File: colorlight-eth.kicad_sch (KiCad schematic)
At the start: 8 parts, among them J1 Conn_02x15_Odd_Even, J2 2250013-4, J4 Conn_01x05_Male, J5 2250013-4

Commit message: v1.2 : fix 5V feed to magnetics
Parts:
- added JP1: SolderJumper_3_Open, Jumper:SolderJumper-3_P1.3mm_Open_RoundedPad1.0x1.5mm, symbol keyboard-rescue:SolderJumper_3_Open-Jumper
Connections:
- net 0V: no longer J1.15 (Pin_15)
- net 3V3: now also JP1.1 (A); no longer J2.2 (VCC), J5.2 (VCC)
- new net 5V: J1.15 (Pin_15), JP1.3 (B)
- new net Vcc: J2.2 (VCC), J5.2 (VCC), JP1.2 (C)
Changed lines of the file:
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@@
   (no_connect (at 211.582 88.392))
   (no_connect (at 110.744 67.818))
+  (wire (pts (xy 124.587 117.729) (xy 128.397 117.729))
+    (stroke (width 0) (type default) (color 0 0 0 0))
+  )
   (wire (pts (xy 208.788 50.292) (xy 211.582 50.292))
     (stroke (width 0) (type default) (color 0 0 0 0))
@@
     (stroke (width 0) (type default) (color 0 0 0 0))
   )
+  (wire (pts (xy 128.397 112.649) (xy 132.08 112.649))
+    (stroke (width 0) (type default) (color 0 0 0 0))
+  )
+  (wire (pts (xy 128.397 115.189) (xy 132.08 115.189))
+    (stroke (width 0) (type default) (color 0 0 0 0))
+  )
   (wire (pts (xy 95.758 60.198) (xy 98.044 60.198))
     (stroke (width 0) (type default) (color 0 0 0 0))
@@
     (stroke (width 0) (type default) (color 0 0 0 0))
   )
+  (wire (pts (xy 128.397 107.569) (xy 128.397 110.109))
+    (stroke (width 0) (type default) (color 0 0 0 0))
+  )
   (wire (pts (xy 208.788 93.472) (xy 211.582 93.472))
     (stroke (width 0) (type default) (color 0 0 0 0))
   )
-  (wire (pts (xy 149.606 38.608) (xy 152.4 38.608))
-    (stroke (width 0) (type default) (color 0 0 0 0))
-  )
   (wire (pts (xy 198.628 74.422) (xy 199.898 74.422))
     (stroke (width 0) (type default) (color 0 0 0 0))
@@
     (stroke (width 0) (type default) (color 0 0 0 0))
   )
+  (wire (pts (xy 128.397 110.109) (xy 132.08 110.109))
+    (stroke (width 0) (type default) (color 0 0 0 0))
+  )
   (wire (pts (xy 208.788 75.692) (xy 211.582 75.692))
     (stroke (width 0) (type default) (color 0 0 0 0))
@@
     (stroke (width 0) (type default) (color 0 0 0 0))
   )
+  (wire (pts (xy 128.397 117.729) (xy 128.397 115.189))
+    (stroke (width 0) (type default) (color 0 0 0 0))
+  )
   (wire (pts (xy 199.898 74.422) (xy 199.898 75.692))
     (stroke (width 0) (type default) (color 0 0 0 0))
@@
     (stroke (width 0) (type default) (color 0 0 0 0))
   )
+  (wire (pts (xy 149.352 38.608) (xy 152.4 38.608))
+    (stroke (width 0) (type default) (color 0 0 0 0))
+  )
   (wire (pts (xy 208.788 73.152) (xy 211.582 73.152))
     (stroke (width 0) (type default) (color 0 0 0 0))
@@
     (stroke (width 0) (type default) (color 0 0 0 0))
   )
+  (wire (pts (xy 124.587 107.569) (xy 128.397 107.569))
+    (stroke (width 0) (type default) (color 0 0 0 0))
+  )
   (wire (pts (xy 208.788 47.752) (xy 211.582 47.752))
     (stroke (width 0) (type default) (color 0 0 0 0))
@@
     (stroke (width 0) (type default) (color 0 0 0 0))
   )
+  (global_label "3V3" (shape input) (at 132.08 115.189 0) (fields_autoplaced)
+    (effects (font (size 1.27 1.27)) (justify left))
+    (property "Intersheet References" "${INTERSHEET_REFS}" (id 0) (at 138.0007 115.1096 0)
+      (effects (font (size 1.27 1.27)) (justify left) hide)
+    )
+  )
   (global_label "3V3" (shape input) (at 95.25 88.138 180) (fields_autoplaced)
     (effects (font (size 1.27 1.27)) (justify right))
@@
     )
   )
+  (global_label "Vcc" (shape input) (at 132.08 112.649 0) (fields_autoplaced)
+    (effects (font (size 1.27 1.27)) (justify left))
+    (property "Intersheet References" "${INTERSHEET_REFS}" (id 0) (at 137.7588 112.7284 0)
+      (effects (font (size 1.27 1.27)) (justify left) hide)
+    )
+  )
   (global_label "ETH2_2P" (shape input) (at 95.25 83.058 180) (fields_autoplaced)
     (effects (font (size 1.27 1.27)) (justify right))
@@
     )
   )
-  (global_label "0V" (shape input) (at 95.25 70.358 180) (fields_autoplaced)
-    (effects (font (size 1.27 1.27)) (justify right))
-    (property "Intersheet References" "${INTERSHEET_REFS}" (id 0) (at 90.5388 70.4374 0)
+  (global_label "5V" (shape input) (at 95.25 70.358 180) (fields_autoplaced)
+    (effects (font (size 1.27 1.27)) (justify right))
+    (property "Intersheet References" "${INTERSHEET_REFS}" (id 0) (at 90.5388 70.2786 0)
       (effects (font (size 1.27 1.27)) (justify right) hide)
     )
@@
     )
   )
-  (global_label "3V3" (shape input) (at 208.788 37.592 180) (fields_autoplaced)
-    (effects (font (size 1.27 1.27)) (justify right))
-    (property "Intersheet References" "${INTERSHEET_REFS}" (id 0) (at 202.8673 37.6714 0)
-      (effects (font (size 1.27 1.27)) (justify right) hide)
-    )
-  )
   (global_label "ETH2_2N" (shape input) (at 208.788 47.752 180) (fields_autoplaced)
     (effects (font (size 1.27 1.27)) (justify right))
@@
     )
   )
-  (global_label "3V3" (shape input) (at 149.606 38.608 180) (fields_autoplaced)
-    (effects (font (size 1.27 1.27)) (justify right))
-    (property "Intersheet References" "${INTERSHEET_REFS}" (id 0) (at 143.6853 38.6874 0)
-      (effects (font (size 1.27 1.27)) (justify right) hide)
+  (global_label "5V" (shape input) (at 132.08 110.109 0) (fields_autoplaced)
+    (effects (font (size 1.27 1.27)) (justify left))
+    (property "Intersheet References" "${INTERSHEET_REFS}" (id 0) (at 136.7912 110.1884 0)
+      (effects (font (size 1.27 1.27)) (justify left) hide)
     )
   )
@@
     )
   )
+  (global_label "Vcc" (shape input) (at 208.788 37.592 180) (fields_autoplaced)
+    (effects (font (size 1.27 1.27)) (justify right))
+    (property "Intersheet References" "${INTERSHEET_REFS}" (id 0) (at 203.1092 37.5126 0)
+      (effects (font (size 1.27 1.27)) (justify right) hide)
+    )
+  )
   (global_label "0V" (shape input) (at 95.758 62.738 180) (fields_autoplaced)
     (effects (font (size 1.27 1.27)) (justify right))
@@
     (effects (font (size 1.27 1.27)) (justify right))
     (property "Intersheet References" "${INTERSHEET_REFS}" (id 0) (at 198.2711 45.1326 0)
+      (effects (font (size 1.27 1.27)) (justify right) hide)
+    )
+  )
+  (global_label "Vcc" (shape input) (at 149.352 38.608 180) (fields_autoplaced)
+    (effects (font (size 1.27 1.27)) (justify right))
+    (property "Intersheet References" "${INTERSHEET_REFS}" (id 0) (at 143.6732 38.5286 0)
       (effects (font (size 1.27 1.27)) (justify right) hide)
     )
@@
     (pin "4")
     (pin "5")
+  )
+  (symbol (lib_id "keyboard-rescue:SolderJumper_3_Open-Jumper") (at 124.587 112.649 90) (unit 1)
+    (in_bom yes) (on_board yes)
+    (property "Reference" "JP1" (id 0) (at 128.397 108.839 0))
+    (property "Value" "SolderJumper_3_Open" (id 1) (at 111.379 112.395 90))
+    (property "Footprint" "Jumper:SolderJumper-3_P1.3mm_Open_RoundedPad1.0x1.5mm" (id 2) (at 124.587 112.649 0)
+      (effects (font (size 1.27 1.27)) hide)
+    )
+    (property "Datasheet" "~" (id 3) (at 124.587 112.649 0)
+      (effects (font (size 1.27 1.27)) hide)
+    )
+    (pin "1")
+    (pin "2")
+    (pin "3")
   )
   (symbol (lib_id "Connector_Generic:Conn_02x15_Odd_Even") (at 103.124 70.358 0) (unit 1)
@@
       (reference "J5") (unit 1) (value "2250013-4") (footprint "kicad-lib:BEL_2250013-4")
     )
+    (path "/72234a74-44eb-4a6d-9fba-116b9d661013"
+      (reference "JP1") (unit 1) (value "SolderJumper_3_Open") (footprint "Jumper:SolderJumper-3_P1.3mm_Open_RoundedPad1.0x1.5mm")
+    )
     (path "/51d2f55f-f421-4143-ad5b-a6d529c0c61f"

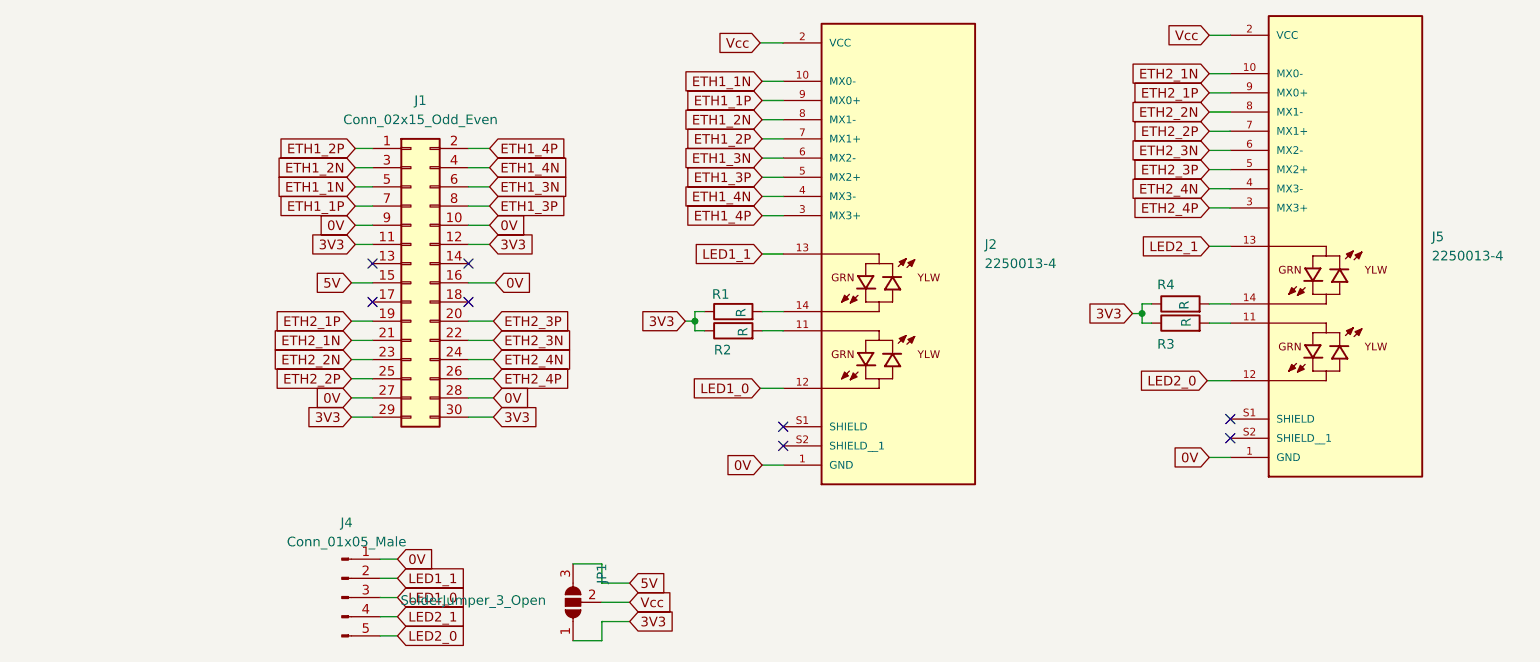
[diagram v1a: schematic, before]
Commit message: v 1.3 : mirrored connector pins
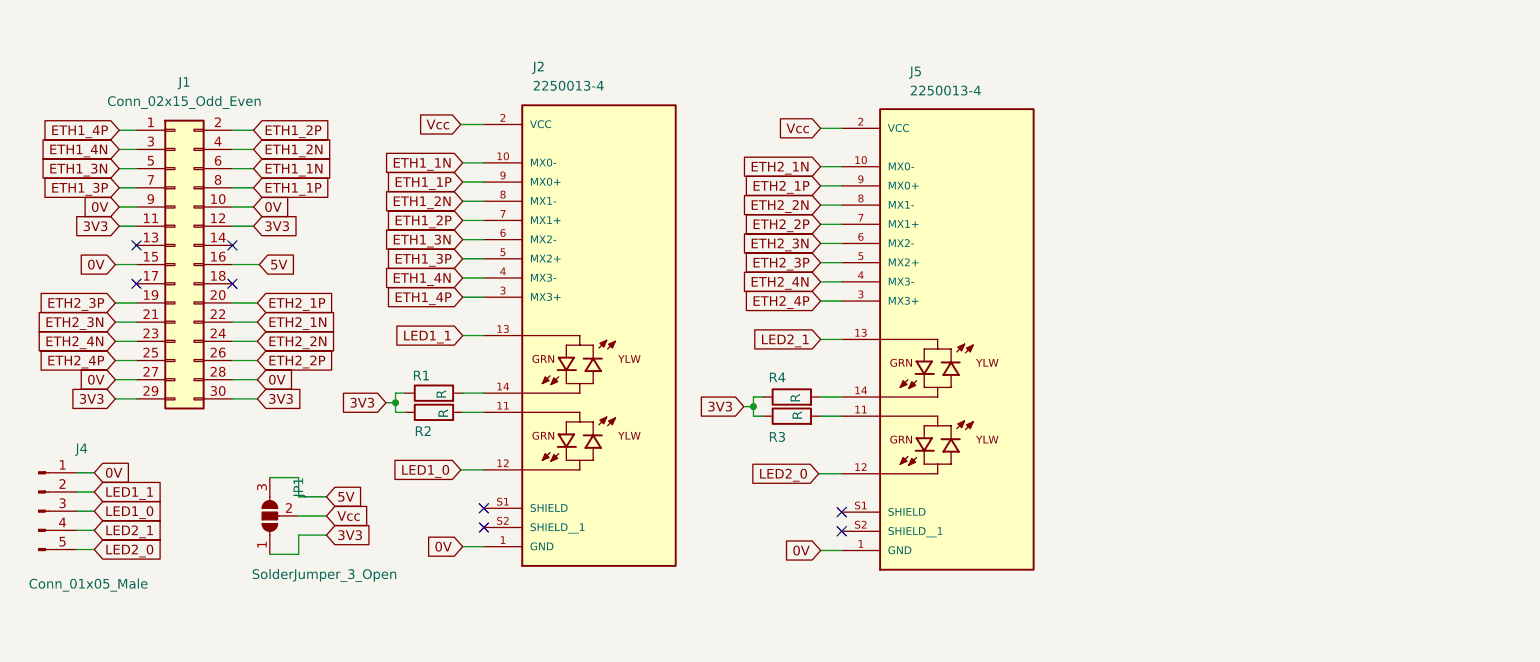
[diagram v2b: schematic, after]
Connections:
- net 0V: now also J1.15 (Pin_15); no longer J1.16 (Pin_16)
- net 5V: now also J1.16 (Pin_16); no longer J1.15 (Pin_15)
- net ETH1_1N: now also J1.6 (Pin_6); no longer J1.5 (Pin_5)
- net ETH1_1P: now also J1.8 (Pin_8); no longer J1.7 (Pin_7)
- net ETH1_2N: now also J1.4 (Pin_4); no longer J1.3 (Pin_3)
- net ETH1_2P: now also J1.2 (Pin_2); no longer J1.1 (Pin_1)
- net ETH1_3N: now also J1.5 (Pin_5); no longer J1.6 (Pin_6)
- net ETH1_3P: now also J1.7 (Pin_7); no longer J1.8 (Pin_8)
- net ETH1_4N: now also J1.3 (Pin_3); no longer J1.4 (Pin_4)
- net ETH1_4P: now also J1.1 (Pin_1); no longer J1.2 (Pin_2)
- net ETH2_1N: now also J1.22 (Pin_22); no longer J1.21 (Pin_21)
- net ETH2_1P: now also J1.20 (Pin_20); no longer J1.19 (Pin_19)
- net ETH2_2N: now also J1.24 (Pin_24); no longer J1.23 (Pin_23)
- net ETH2_2P: now also J1.26 (Pin_26); no longer J1.25 (Pin_25)
- net ETH2_3N: now also J1.21 (Pin_21); no longer J1.22 (Pin_22)
- net ETH2_3P: now also J1.19 (Pin_19); no longer J1.20 (Pin_20)
- net ETH2_4N: now also J1.23 (Pin_23); no longer J1.24 (Pin_24)
- net ETH2_4P: now also J1.25 (Pin_25); no longer J1.26 (Pin_26)
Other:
- moved on the sheet: J1, J2, J4, J5, JP1, R1, R2, R3, R4
